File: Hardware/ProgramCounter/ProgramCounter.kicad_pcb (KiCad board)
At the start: 4 copper layers, 90 x 55 mm, 35 parts, among them J1 Conn_02x08, J2 Conn_02x08, J3 Conn_02x08, J4 Conn_02x08

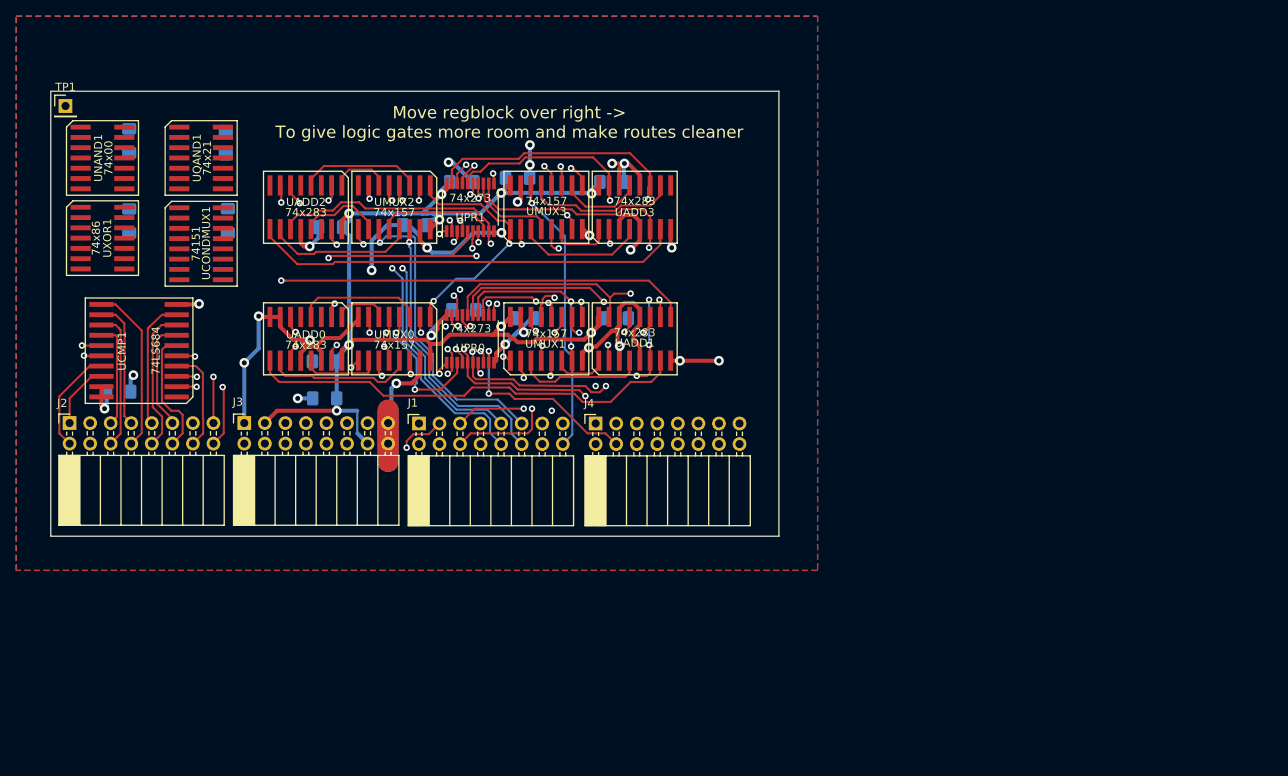
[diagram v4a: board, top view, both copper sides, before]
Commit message: Program Counter Board
Seems to be done. Likely be ordering very soon. Also added a debug/testpoint connector to the top so that I can probe it easier
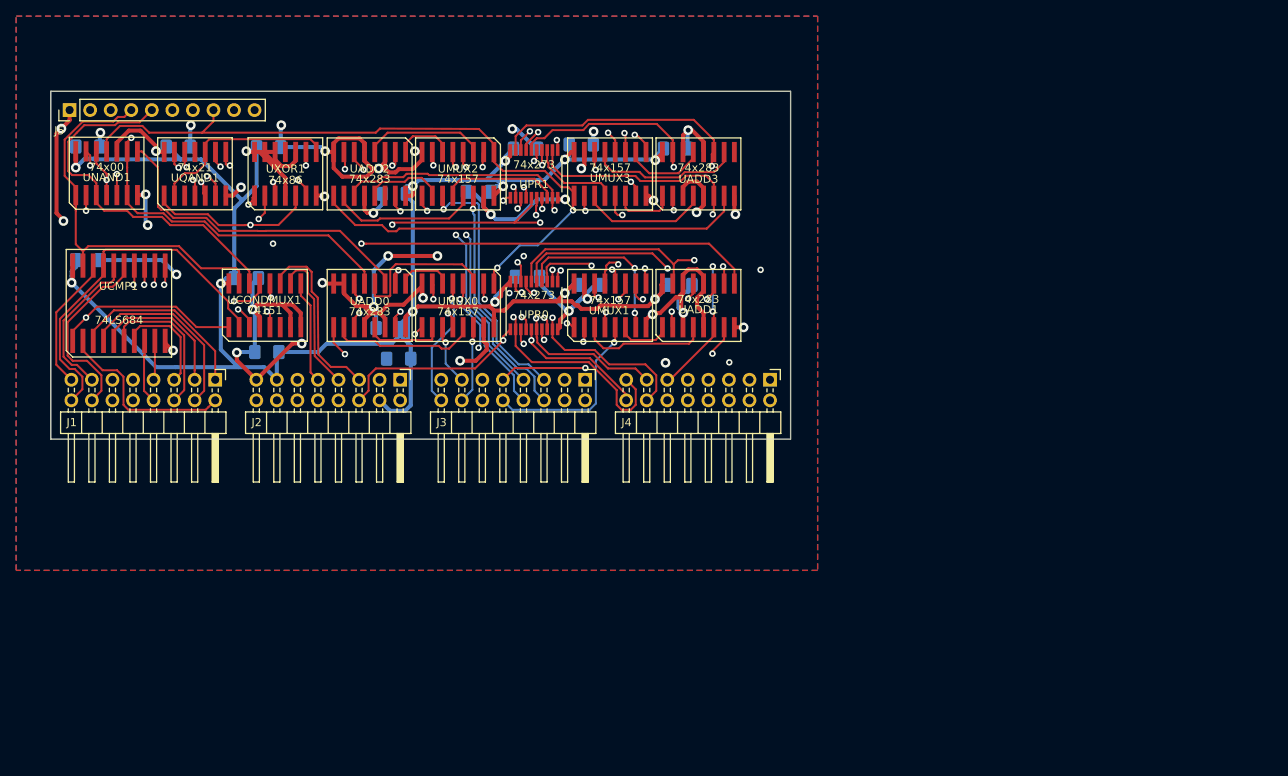
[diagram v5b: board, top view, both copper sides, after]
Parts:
- removed TP1: TP_PCEVENT, Connector_PinHeader_2.54mm:PinHeader_1x01_P2.54mm_Vertical
- added C16: .1uF, Capacitor_SMD:C_1206_3216Metric_Pad1.42x1.75mm_HandSolder, B.Cu at (93.0, 83.1)
- added J5: Conn_01x10_Male, Connector_PinHeader_2.54mm:PinHeader_1x10_P2.54mm_Vertical, F.Cu at (52.3, 52.3)
- J1: renamed from J2; footprint Connector_PinSocket_2.54mm:PinSocket_2x08_P2.54mm_Horizontal -> Connector_PinHeader_2.54mm:PinHeader_2x08_P2.54mm_Horizontal
- J2: renamed from J3; footprint Connector_PinSocket_2.54mm:PinSocket_2x08_P2.54mm_Horizontal -> Connector_PinHeader_2.54mm:PinHeader_2x08_P2.54mm_Horizontal
- J3: renamed from J1; footprint Connector_PinSocket_2.54mm:PinSocket_2x08_P2.54mm_Horizontal -> Connector_PinHeader_2.54mm:PinHeader_2x08_P2.54mm_Horizontal
- J4: footprint Connector_PinSocket_2.54mm:PinSocket_2x08_P2.54mm_Horizontal -> Connector_PinHeader_2.54mm:PinHeader_2x08_P2.54mm_Horizontal
- moved UXOR1 24.0 mm to (79.0, 60.2), turned to 0 degrees
- moved J4 22.2 mm to (138.9, 85.7), turned to 270 degrees
- moved J3 21.2 mm to (116.0, 85.7), turned to 270 degrees
- moved J2 20.0 mm to (93.2, 85.7), turned to 270 degrees
- moved J1 18.8 mm to (70.3, 85.7), turned to 270 degrees
- moved C5 16.7 mm to (54.6, 70.9)
- moved C13 16.1 mm to (74.2, 73.1), turned to 0 degrees
- moved UCONDMUX1 10.9 mm to (76.5, 76.5), turned to 0 degrees
- moved C3 10.4 mm to (76.9, 56.9), turned to 0 degrees
- moved C9 9.16 mm to (76.7, 82.2)
- moved C11 8.89 mm to (92.5, 62.7)
- moved C14 8.89 mm to (102.9, 62.4)
- moved C2 8.89 mm to (108.9, 72.9)
- moved UMUX1 8.89 mm to (119.1, 76.5)
- moved UMUX3 8.89 mm to (119.1, 60.2)
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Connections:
- J1 pad 1: /RCD7 -> /RCD0
- J1 pad 10: /RCS3 -> /RCS4
- J1 pad 11: /RCD2 -> /RCD5
- J1 pad 12: /RCS2 -> /RCS5
- J1 pad 13: /RCD1 -> /RCD6
- J1 pad 14: /RCS1 -> /RCS6
- J1 pad 15: /RCD0 -> /RCD7
- J1 pad 16: /RCS0 -> /RCS7
- J1 pad 2: /RCS7 -> /RCS0
- J1 pad 3: /RCD6 -> /RCD1
- J1 pad 4: /RCS6 -> /RCS1
- J1 pad 5: /RCD5 -> /RCD2
- J1 pad 6: /RCS5 -> /RCS2
- J1 pad 7: /RCD4 -> /RCD3
- J1 pad 8: /RCS4 -> /RCS3
- J1 pad 9: /RCD3 -> /RCD4
- J2 pad 10: /CLK_WB -> /OPCODE3
- J2 pad 11: /IMM1 -> /FLAG_CARRY
- J2 pad 12: /~RST -> /OPCODE2
- J2 pad 13: /IMM0 -> VCC
- J2 pad 14: VCC -> /OPCODE1
- J2 pad 16: GND -> /OPCODE0
- J2 pad 2: /OPCODE0 -> GND
- J2 pad 3: VCC -> /IMM0
- J2 pad 4: /OPCODE1 -> VCC
- J2 pad 5: /FLAG_CARRY -> /IMM1
- J2 pad 6: /OPCODE2 -> /~RST
- J2 pad 7: /IMM3 -> /IMM2
- J2 pad 8: /OPCODE3 -> /CLK_WB
- J2 pad 9: /IMM2 -> /IMM3
- J3 pad 1: /REGMEM0 -> /REGMEM14
- J3 pad 10: /REGMEM9 -> /REGMEM5
- J3 pad 11: /REGMEM10 -> /REGMEM4
- J3 pad 12: /REGMEM11 -> /REGMEM7
- J3 pad 13: /REGMEM12 -> /REGMEM2
- J3 pad 14: /REGMEM13 -> /REGMEM3
- J3 pad 15: /REGMEM14 -> /REGMEM0
- J3 pad 16: /REGMEM15 -> /REGMEM1
- J3 pad 2: /REGMEM1 -> /REGMEM15
- J3 pad 3: /REGMEM2 -> /REGMEM12
- J3 pad 4: /REGMEM3 -> /REGMEM13
- J3 pad 5: /REGMEM4 -> /REGMEM10
- J3 pad 6: /REGMEM7 -> /REGMEM11
- J3 pad 7: /REGMEM6 -> /REGMEM8
- J3 pad 8: /REGMEM5 -> /REGMEM9
- J3 pad 9: /REGMEM8 -> /REGMEM6
- J4 pad 1: /PCOUT0 -> /PCOUT14
- J4 pad 10: /PCOUT9 -> /PCOUT7
- J4 pad 11: /PCOUT10 -> /PCOUT4
- J4 pad 12: /PCOUT11 -> /PCOUT5
- J4 pad 13: /PCOUT12 -> /PCOUT2
- J4 pad 14: /PCOUT13 -> /PCOUT3
- J4 pad 15: /PCOUT14 -> /PCOUT0
- J4 pad 16: /PCOUT15 -> /PCOUT1
- J4 pad 2: /PCOUT1 -> /PCOUT15
- J4 pad 3: /PCOUT2 -> /PCOUT12
- J4 pad 4: /PCOUT3 -> /PCOUT13
- J4 pad 5: /PCOUT4 -> /PCOUT10
- J4 pad 6: /PCOUT5 -> /PCOUT11
- J4 pad 7: /PCOUT6 -> /PCOUT8
- J4 pad 8: /PCOUT7 -> /PCOUT9
- J4 pad 9: /PCOUT8 -> /PCOUT6
- UCONDMUX1 pad 3: GND -> /NEWCOND
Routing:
- net VCC: track 175.9 -> 293.8 mm, vias 11 -> 14
- net GND: track 184.7 -> 301.7 mm, vias 26 -> 39
- net /~IS_JMP: track 42.1 -> 97.8 mm
- net /cmpgt: track 0.00 -> 51.8 mm, vias 0 -> 2
- net /cmpeq: track 0.00 -> 51.3 mm
- net /~IS_SKIP: track 0.00 -> 49.1 mm, vias 0 -> 1
- net /cmplt: track 0.00 -> 46.1 mm
- net /OPCODE0: track 0.00 -> 45.2 mm, vias 0 -> 1
- net /OPCODE2: track 0.00 -> 44.4 mm, vias 0 -> 2
- net /OPCODE3: track 0.00 -> 42.9 mm, vias 0 -> 2
- net /IS_SKIP: track 0.00 -> 40.8 mm
- net /PCEVENT: track 0.00 -> 39.9 mm, vias 0 -> 2
- net /NEWCOND: track 0.00 -> 35.3 mm, vias 0 -> 1
- net /OPCODE1: track 0.00 -> 33.5 mm, vias 0 -> 2
- net /RCS7: track 13.2 -> 44.6 mm
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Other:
- board size 90 x 55 mm -> 91.4 x 43 mm
- board text added: "5V/INST/ETC"
- board text added: "PCOUT"
- board text added: "RCS/RCD"
- board text added: "REGMEM"
- board text removed: "Move regblock over right -> To give logic gates more room and make routes cleaner"

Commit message: Motherboard Significant Progress
This involves significant buildup of the motherboard, such as the power, oscillator, and overall design.

The motherboard schematic is in progress (some lines have yet to be connected), and the PCB layout is mostly just there to consider spacing.
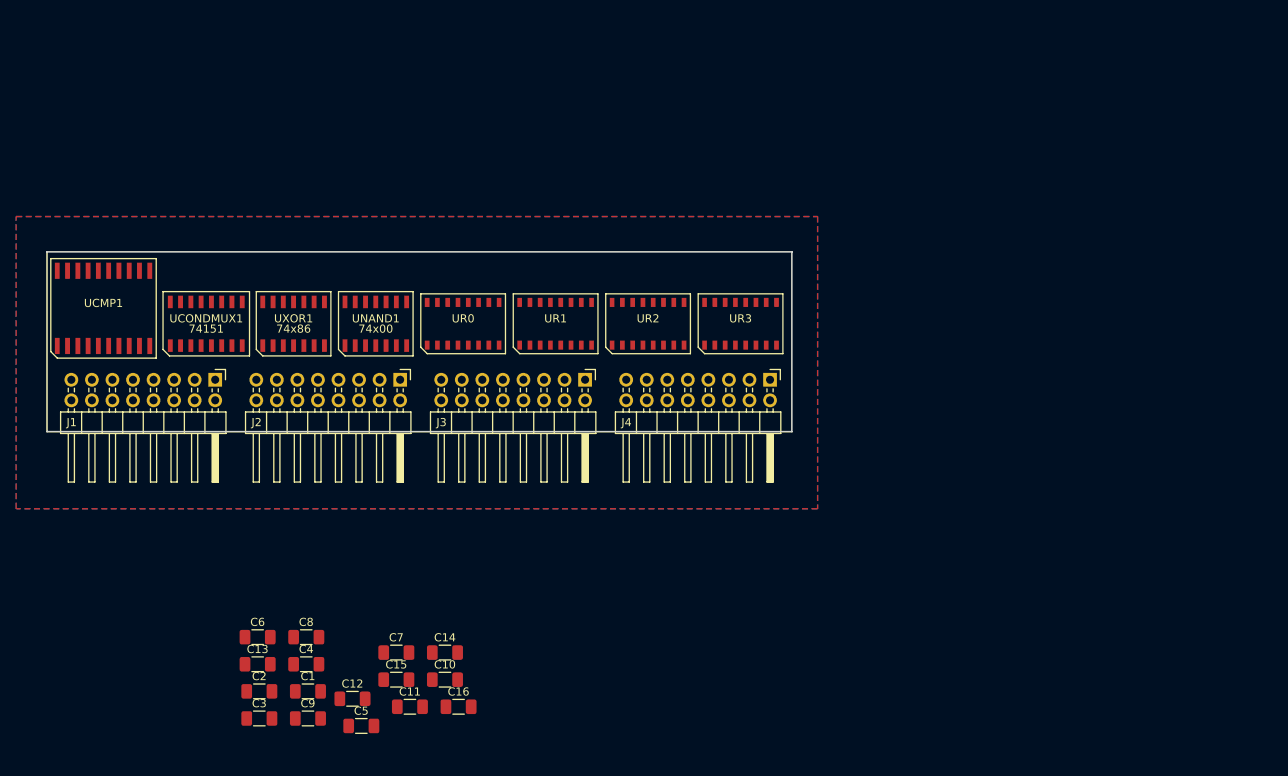
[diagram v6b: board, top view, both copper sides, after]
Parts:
- removed J5: Conn_01x10_Male, Connector_PinHeader_2.54mm:PinHeader_1x10_P2.54mm_Vertical
- removed UADD0, UADD1, UADD2, UADD3: 74x283, aFootprint:R-PDSO-G16
- removed UMUX0, UMUX1, UMUX2, UMUX3: 74x157, aFootprint:R-PDSO-G16
- removed UPR0, UPR1: 74x273, Package_SO:TSSOP-20_4.4x6.5mm_P0.65mm
- removed UQAND1: 74x21, aFootprint:R-PDSO-G14
- added UR0: 74LS161, 000custom:SOIC16-ONSEMI_751B-05_K, F.Cu at (101.0, 78.7)
- added UR1: 74LS161, 000custom:SOIC16-ONSEMI_751B-05_K, F.Cu at (112.4, 78.7)
- added UR2: 74LS161, 000custom:SOIC16-ONSEMI_751B-05_K, F.Cu at (123.8, 78.7)
- added UR3: 74LS161, 000custom:SOIC16-ONSEMI_751B-05_K, F.Cu at (135.3, 78.7)
- C1, C10, C11, C12, C13, C14, C15, C16, C2, C3, C4, C5, C6, C7, C8, C9: footprint Capacitor_SMD:C_1206_3216Metric_Pad1.42x1.75mm_HandSolder -> Capacitor_SMD:C_1206_3216Metric_Pad1.33x1.80mm_HandSolder; moved to F.Cu
- UCMP1: footprint aFootprint:DW0020A -> 000custom:SOIC20_TI_DW0020A
- UCONDMUX1: footprint aFootprint:R-PDSO-G16 -> 000custom:D_R-PDSO-G16
- UNAND1, UXOR1: footprint aFootprint:R-PDSO-G14 -> 000custom:D_R-PDSO-G14
- moved C12 71.6 mm to (87.3, 125.1)
- moved C10 71.6 mm to (98.7, 122.7)
- moved C3 70.6 mm to (75.8, 127.5)
- moved C15 70.0 mm to (92.7, 122.7)
- moved C4 69.5 mm to (81.6, 120.8)
- moved C5 66.8 mm to (88.4, 128.4)
- moved C7 64.3 mm to (92.7, 119.4)
- moved C8 63.5 mm to (81.6, 117.5)
- moved C11 63.4 mm to (94.4, 126.1), turned to 0 degrees
- moved C2 61.0 mm to (75.8, 124.2)
- moved C6 59.8 mm to (75.6, 117.5)
- moved C14 57.1 mm to (98.7, 119.4), turned to 0 degrees
- moved C13 47.8 mm to (75.6, 120.8)
- moved C1 46.0 mm to (81.8, 124.2), turned to 0 degrees
- moved C9 45.6 mm to (81.8, 127.5), turned to 0 degrees
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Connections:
- net /~IS_SKIP renamed /~{IS_SKIP}
- J2 pad 10: /OPCODE3 -> /IS_SKIP
- J2 pad 12: /OPCODE2 -> /SINST
- J2 pad 14: /OPCODE1 -> /JINST
- J2 pad 16: /OPCODE0 -> /CEP
- J2 pad 6: /~RST -> /~{RST}
- J3 pad 1: /REGMEM14 -> /REGMEM7
- J3 pad 10: /REGMEM5 -> /PCOUT3
- J3 pad 11: /REGMEM4 -> /REGMEM2
- J3 pad 12: /REGMEM7 -> /PCOUT2
- J3 pad 13: /REGMEM2 -> /REGMEM1
- J3 pad 14: /REGMEM3 -> /PCOUT1
- J3 pad 16: /REGMEM1 -> /PCOUT0
- J3 pad 2: /REGMEM15 -> /PCOUT7
- J3 pad 3: /REGMEM12 -> /REGMEM6
- J3 pad 4: /REGMEM13 -> /PCOUT6
- J3 pad 5: /REGMEM10 -> /REGMEM5
- J3 pad 6: /REGMEM11 -> /PCOUT5
- J3 pad 7: /REGMEM8 -> /REGMEM4
- J3 pad 8: /REGMEM9 -> /PCOUT4
- J3 pad 9: /REGMEM6 -> /REGMEM3
- J4 pad 1: /PCOUT14 -> /REGMEM15
- J4 pad 10: /PCOUT7 -> /PCOUT11
- J4 pad 11: /PCOUT4 -> /REGMEM10
- J4 pad 12: /PCOUT5 -> /PCOUT10
- J4 pad 13: /PCOUT2 -> /REGMEM9
- J4 pad 14: /PCOUT3 -> /PCOUT9
- J4 pad 15: /PCOUT0 -> /REGMEM8
- J4 pad 16: /PCOUT1 -> /PCOUT8
- J4 pad 3: /PCOUT12 -> /REGMEM14
- J4 pad 4: /PCOUT13 -> /PCOUT14
- J4 pad 5: /PCOUT10 -> /REGMEM13
- J4 pad 6: /PCOUT11 -> /PCOUT13
- J4 pad 7: /PCOUT8 -> /REGMEM12
- J4 pad 8: /PCOUT9 -> /PCOUT12
- J4 pad 9: /PCOUT6 -> /REGMEM11
- UCONDMUX1 pad 6: Net-(UCONDMUX1-Pad6) -> unconnected-(UCONDMUX1-Pad6)
- UNAND1 pad 11: /~IS_JMP -> /~{IS_JMP}
- UNAND1 pad 3: /cmplt -> unconnected-(UNAND1-Pad3)
- UXOR1 pad 10: VCC -> GND
- UXOR1 pad 11: Net-(UXOR1-Pad11) -> unconnected-(UXOR1-Pad11)
- UXOR1 pad 12: VCC -> GND
- UXOR1 pad 13: VCC -> GND
- UXOR1 pad 4: VCC -> GND
- UXOR1 pad 5: /OPCODE0 -> GND
- UXOR1 pad 6: /~OPCODE0 -> unconnected-(UXOR1-Pad6)
- UXOR1 pad 8: /~OPCODE1 -> unconnected-(UXOR1-Pad8)
- UXOR1 pad 9: /OPCODE1 -> GND
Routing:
- net GND: track 301.7 -> 0.00 mm, vias 39 -> 0
- net VCC: track 293.8 -> 0.00 mm, vias 14 -> 0
- net /~IS_JMP: track 97.8 -> 0.00 mm, vias 3 -> 0
- net /PCOUT9: track 79.3 -> 0.00 mm, vias 3 -> 0
- net /PCOUT8: track 75.8 -> 0.00 mm, vias 2 -> 0
- net /PCOUT11: track 75.6 -> 0.00 mm, vias 1 -> 0
- net /PCOUT10: track 66.8 -> 0.00 mm, vias 3 -> 0
- net /PCOUT15: track 64.3 -> 0.00 mm, vias 1 -> 0
- net /16 Bit Adder/CARRY1: track 61.4 -> 0.00 mm, vias 2 -> 0
- net /CLK_WB: track 58.4 -> 0.00 mm, vias 2 -> 0
- net /PCOUT14: track 55.4 -> 0.00 mm, vias 2 -> 0
- net /PCOUT13: track 54.2 -> 0.00 mm, vias 2 -> 0
- net /16 Bit Adder/CARRY0: track 54.0 -> 0.00 mm, vias 2 -> 0
- net /16 Bit Adder/CARRY2: track 53.6 -> 0.00 mm
- net /cmpgt: track 51.8 -> 0.00 mm, vias 2 -> 0
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- added copper zone on B.Cu, net VCC
- removed copper zone on B.Cu, net GND
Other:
- board size 91.4 x 43 mm -> 92.1 x 22.2 mm
- net class Default removed
- net class Power removed
